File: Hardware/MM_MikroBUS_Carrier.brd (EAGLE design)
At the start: 85.1 x 35.6 mm, 106 parts, among them J15 MICROMOD-2222-C, J2 QWIIC_RIGHT_ANGLE, J5 Vertical Qwiic Connector, J7 MIKROBUS_SMD_BLACK1, J9 CORTEX_JTAG_DEBUG_MINIMUM_PTH, U1 MCP73831, U2 AP7361C-33FGEUDFN-8

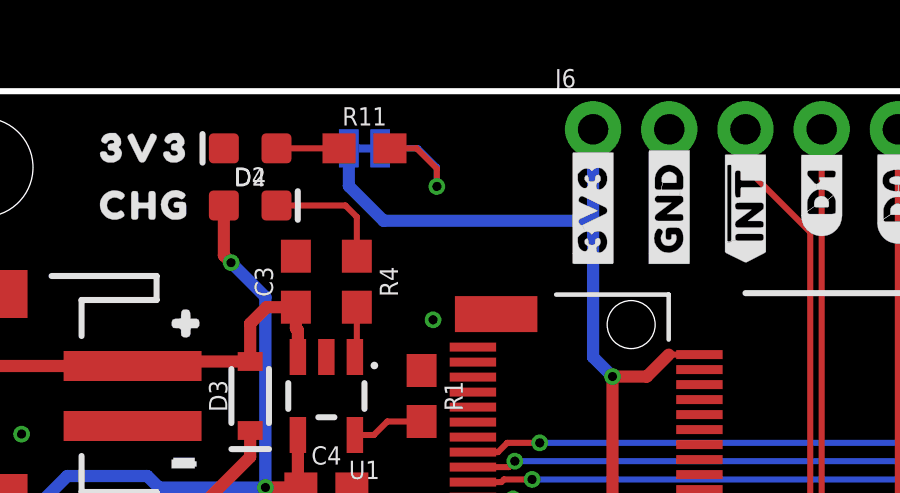
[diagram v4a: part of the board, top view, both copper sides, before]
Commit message: Pete's updates:
* LED jumper label became "3V3LED"
* fuse jumper label became "FUSE_BYP"
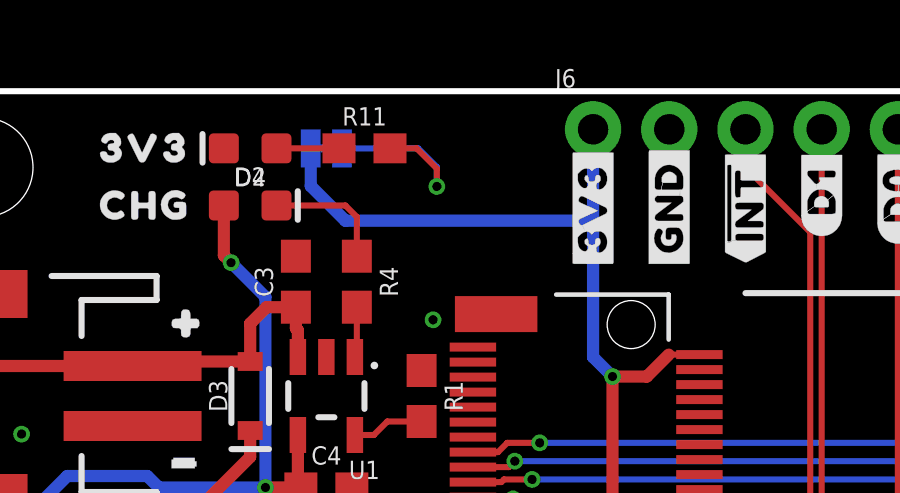
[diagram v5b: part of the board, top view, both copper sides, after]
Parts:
- removed U$7: (no value), output:#BYP#0
- added U$1: (no value), output:#3V3LED#0
- U$19: device output:#3V3_#0 -> output:#FUSE_BYP#0
- moved U$19 12.8 mm to (16.6, 21.6)
- moved JP4 1.27 mm to (14.0, 33.7)
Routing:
- net 3.3V: track 128.0 -> 129.3 mm
- net N$4: track 5.24 -> 6.51 mm
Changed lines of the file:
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@@
 <?xml version="1.0" encoding="utf-8"?>
 <!DOCTYPE eagle SYSTEM "eagle.dtd">
-<eagle version="9.5.2">
+<eagle version="9.6.2">
 <drawing>
 <settings>
-<setting alwaysvectorfont="no"/>
+<setting alwaysvectorfont="yes"/>
 <setting verticaltext="up"/>
 </settings>
@@
 <attribute name="PROD_ID" value="HW-14899" x="44.327" y="13.76" size="1.778" layer="27" font="vector" ratio="15" display="off"/>
 </element>
-<element name="JP4" library="SparkFun-Jumpers" package="SMT-JUMPER_2_NC_TRACE_SILK" package3d_urn="urn:adsk.eagle:package:39281/1" value="3V3 LED" x="15.24" y="33.655" smashed="yes" rot="MR0">
-<attribute name="NAME" x="15.24" y="34.798" size="0.6096" layer="26" font="vector" ratio="20" rot="MR0" align="bottom-center"/>
-<attribute name="VALUE" x="15.24" y="32.512" size="0.6096" layer="28" font="vector" ratio="20" rot="MR0" align="top-center"/>
+<element name="JP4" library="SparkFun-Jumpers" package="SMT-JUMPER_2_NC_TRACE_SILK" package3d_urn="urn:adsk.eagle:package:39281/1" value="3V3 LED" x="13.97" y="33.655" smashed="yes" rot="MR0">
+<attribute name="NAME" x="13.97" y="34.798" size="0.6096" layer="26" font="vector" ratio="20" rot="MR0" align="bottom-center"/>
+<attribute name="VALUE" x="13.97" y="32.512" size="0.6096" layer="28" font="vector" ratio="20" rot="MR0" align="top-center"/>
 </element>
 <element name="R11" library="SparkFun-Resistors" package="0603" value="1k" x="15.24" y="33.655" smashed="yes">
@@
 </element>
 <element name="U$4" library="output" package="CHG0" value="" x="5.715" y="31.75" smashed="yes"/>
-<element name="U$7" library="output" package="#BYP#0" value="" x="11.684" y="21.463" smashed="yes" rot="MR0"/>
 <element name="U$9" library="output" package="#MEAS#0" value="" x="16.51" y="7.874" smashed="yes" rot="MR0"/>
 <element name="J4" library="SparkFun-Connectors" package="1X02_NO_SILK" value="" x="1.27" y="19.685" smashed="yes" rot="R270">
@@
 <element name="U$10" library="output" package="#3V3#0" value="" x="22.86" y="29.464" smashed="yes" rot="R90"/>
 <element name="U$13" library="output" package="#3V3#0" value="" x="22.86" y="29.464" smashed="yes" rot="MR90"/>
-<element name="U$19" library="output" package="#3V3_#0" value="" x="20.828" y="33.655" smashed="yes" rot="MR0"/>
 <element name="U$6" library="output" package="#3V3_EN#0" value="" x="15.748" y="16.51" smashed="yes" rot="MR0"/>
 <element name="U$5" library="output" package="MIKROBUS_CARRIER0" value="" x="57.531" y="1.651" smashed="yes"/>
@@
 <element name="SWDCK" library="SparkFun-Connectors" package="PAD.03X.03" value="TEST-POINT3" x="33.02" y="6.35" smashed="yes"/>
 <element name="SWDIO" library="SparkFun-Connectors" package="PAD.03X.03" value="TEST-POINT3" x="30.48" y="6.35" smashed="yes"/>
+<element name="U$1" library="output" package="#3V3LED#0" value="" x="21.971" y="33.528" smashed="yes" rot="MR0"/>
+<element name="U$19" library="output" package="#FUSE_BYP#0" value="" x="16.637" y="21.59" smashed="yes" rot="MR0"/>
 </elements>
 <signals>
@@
 <wire x1="23.00049375" y1="8.87650625" x2="22.987" y2="8.89" width="0.2032" layer="16"/>
 <wire x1="22.987" y1="8.89" x2="21.336" y2="8.89" width="0.4064" layer="16"/>
-<wire x1="14.7193" y1="33.655" x2="14.7193" y2="32.3977" width="0.4064" layer="16"/>
-<wire x1="14.7193" y1="32.3977" x2="15.875" y2="31.242" width="0.4064" layer="16"/>
+<wire x1="14.605" y1="31.242" x2="13.4493" y2="32.3977" width="0.4064" layer="16"/>
+<wire x1="13.4493" y1="33.655" x2="13.4493" y2="32.3977" width="0.4064" layer="16"/>
 <wire x1="23.5077" y1="26.0477" x2="23.5077" y2="12.4317125" width="0.4064" layer="1"/>
 <wire x1="23.00049375" y1="8.87650625" x2="23.00049375" y2="11.92450625" width="0.4064" layer="1"/>
@@
 <wire x1="22.86" y1="31.242" x2="22.86" y2="26.6954" width="0.4064" layer="16"/>
 <wire x1="22.86" y1="26.6954" x2="23.5077" y2="26.0477" width="0.4064" layer="16"/>
-<wire x1="15.875" y1="31.242" x2="22.86" y2="31.242" width="0.4064" layer="16"/>
+<wire x1="14.605" y1="31.242" x2="22.86" y2="31.242" width="0.4064" layer="16"/>
 <contactref element="J7" pad="7"/>
 <wire x1="49.246" y1="25.243" x2="50.419" y2="26.416" width="0.4064" layer="1"/>
@@
 <wire x1="17.653" y1="32.385" x2="17.653" y2="33.0327" width="0.2032" layer="16"/>
 <wire x1="17.653" y1="33.0327" x2="17.0307" y2="33.655" width="0.2032" layer="16"/>
-<wire x1="17.0307" y1="33.655" x2="15.7607" y2="33.655" width="0.2032" layer="16"/>
+<wire x1="17.0307" y1="33.655" x2="14.4907" y2="33.655" width="0.2032" layer="16"/>
 </signal>
 <signal name="N$6">

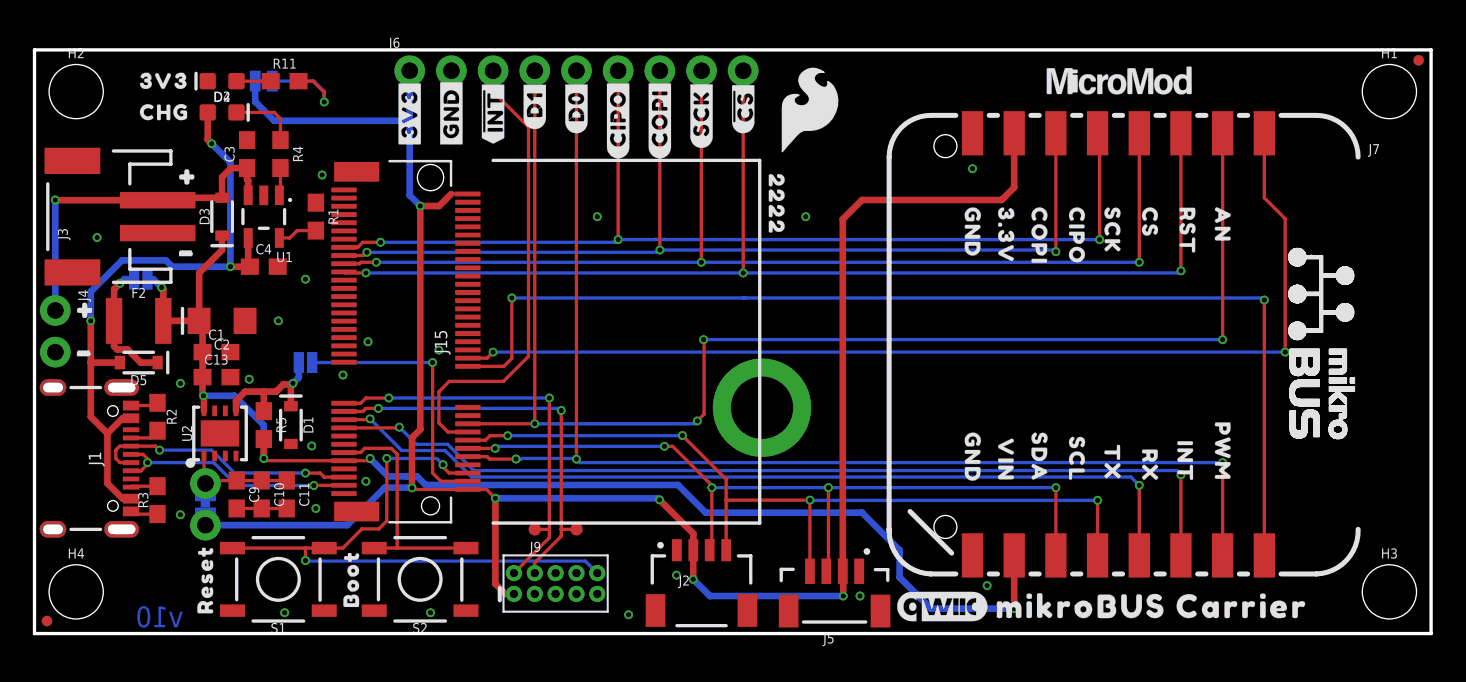
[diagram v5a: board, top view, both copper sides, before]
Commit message: Design review updates:
* Put mikroBUS pin labels into the table
* Add y-measure for mikroBUS socket
* Add mikroBUS logo to library and to the back of the board
* Add GND vias
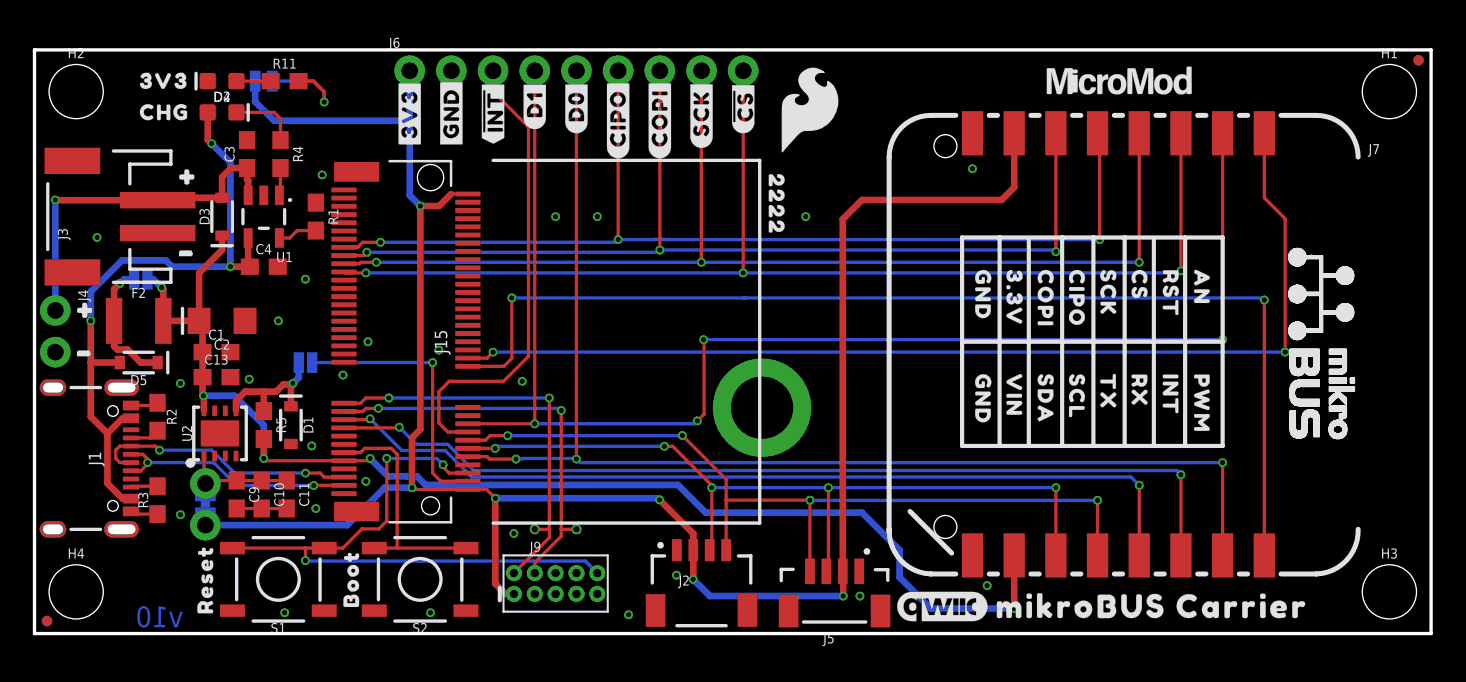
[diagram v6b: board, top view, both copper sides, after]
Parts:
- removed U$38: (no value), output:_MIKROBUS_CARRIER0
- added U$7: MIKROBUS_LOGO, mikroBUS_SMD_BLACK:MIKROBUS_LOGO
- SWDCK, SWDIO: value TEST-POINT3 -> TEST-POINTTP_15TH_THRU; device SparkFun-Connectors:PAD.03X.03 -> SparkFun-Connectors:TP_15TH
- moved U$51 4.62 mm to (67.3, 16.5)
- moved U$52 4.33 mm to (65.4, 16.5)
- moved U$50 4.16 mm to (69.2, 16.5)
- moved U$35 4.02 mm to (71.1, 22.9)
- moved U$55 3.97 mm to (59.7, 16.5)
- moved U$40 3.94 mm to (69.2, 22.9)
- moved U$47 3.86 mm to (57.8, 22.9)
- moved U$41 3.86 mm to (67.3, 22.9)
- moved U$46 3.84 mm to (59.7, 22.9)
- moved U$45 3.83 mm to (61.6, 22.9)
- moved U$42 3.82 mm to (65.4, 22.9)
- moved U$43 3.81 mm to (63.5, 22.9)
- moved U$53 3.81 mm to (63.5, 16.5)
- moved U$48 3.61 mm to (57.8, 16.5)
- moved U$54 3.58 mm to (61.6, 16.5)
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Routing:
- net GND: vias 22 -> 25
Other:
- board text added: "All units in inches."
- board text removed: "in"

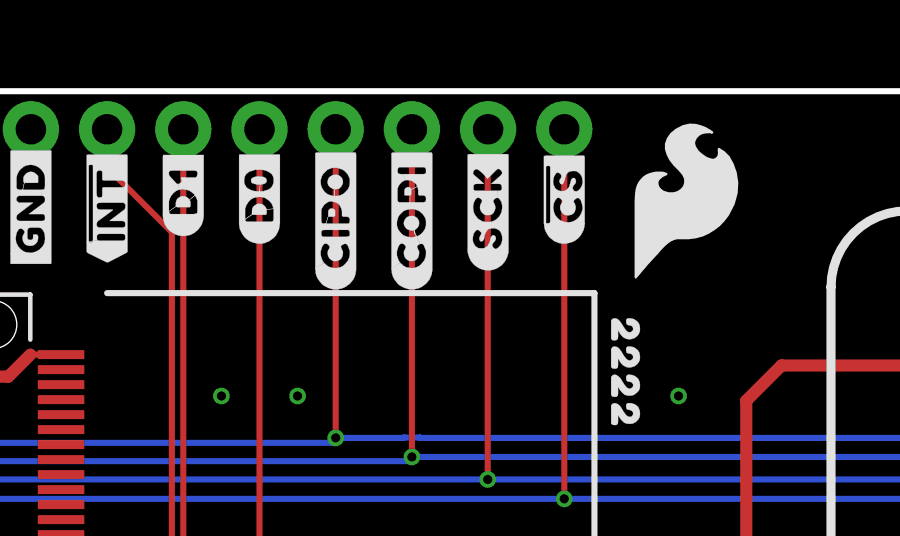
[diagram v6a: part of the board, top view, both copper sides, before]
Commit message: Design review updates
* Add direction to the SPI header labels
* Remove underscores from labels
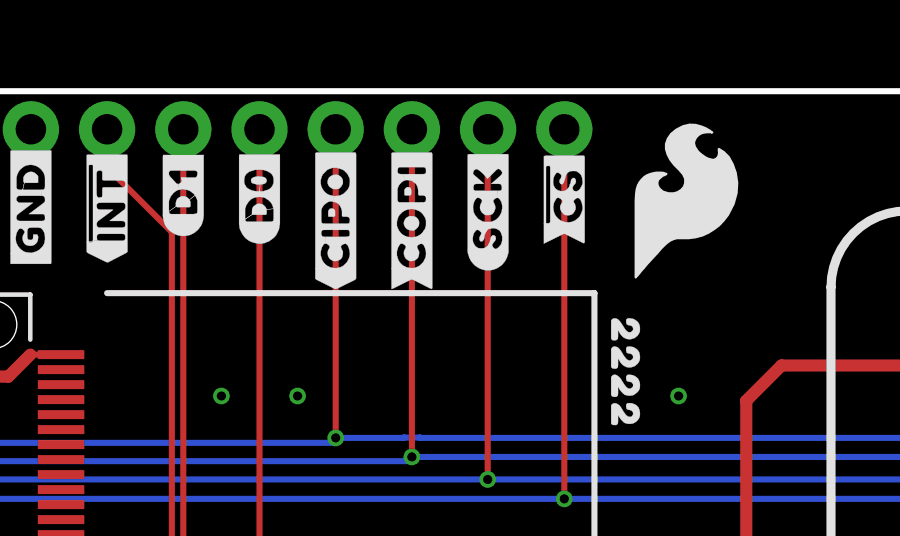
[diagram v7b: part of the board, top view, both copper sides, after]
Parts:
- removed U$19: (no value), output:#FUSE_BYP#0
- removed U$6: (no value), output:#3V3_EN#0
- added U$38: (no value), output:#FUSEBYP#0
- added U$39: (no value), output:#3V3EN#0
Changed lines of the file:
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@@
 <?xml version="1.0" encoding="utf-8"?>
 <!DOCTYPE eagle SYSTEM "eagle.dtd">
-<eagle version="9.5.2">
+<eagle version="9.6.2">
 <drawing>
 <settings>
@@
 <element name="U$10" library="output" package="#3V3#0" value="" x="22.86" y="29.464" smashed="yes" rot="R90"/>
 <element name="U$13" library="output" package="#3V3#0" value="" x="22.86" y="29.464" smashed="yes" rot="MR90"/>
-<element name="U$6" library="output" package="#3V3_EN#0" value="" x="15.748" y="16.51" smashed="yes" rot="MR0"/>
 <element name="U$5" library="output" package="MIKROBUS_CARRIER0" value="" x="57.531" y="1.651" smashed="yes"/>
 <element name="U$35" library="output" package="AN0" value="" x="71.12" y="22.86" smashed="yes" rot="R270"/>
@@
 <element name="SWDIO" library="SparkFun-Connectors" package="TP_15TH" value="TEST-POINTTP_15TH_THRU" x="30.48" y="6.35" smashed="yes"/>
 <element name="U$1" library="output" package="#3V3LED#0" value="" x="21.971" y="33.528" smashed="yes" rot="MR0"/>
-<element name="U$19" library="output" package="#FUSE_BYP#0" value="" x="16.637" y="21.59" smashed="yes" rot="MR0"/>
 <element name="U$7" library="mikroBUS_SMD_BLACK" package="MIKROBUS_LOGO" value="MIKROBUS_LOGO" x="61.087" y="17.018" smashed="yes" rot="MR0"/>
+<element name="U$38" library="output" package="#FUSEBYP#0" value="" x="15.367" y="21.59" smashed="yes" rot="MR0"/>
+<element name="U$39" library="output" package="#3V3EN#0" value="" x="15.748" y="16.51" smashed="yes" rot="MR0"/>
 </elements>
 <signals>
